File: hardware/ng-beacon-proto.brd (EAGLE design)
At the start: 71.1 x 76.2 mm, 6 parts

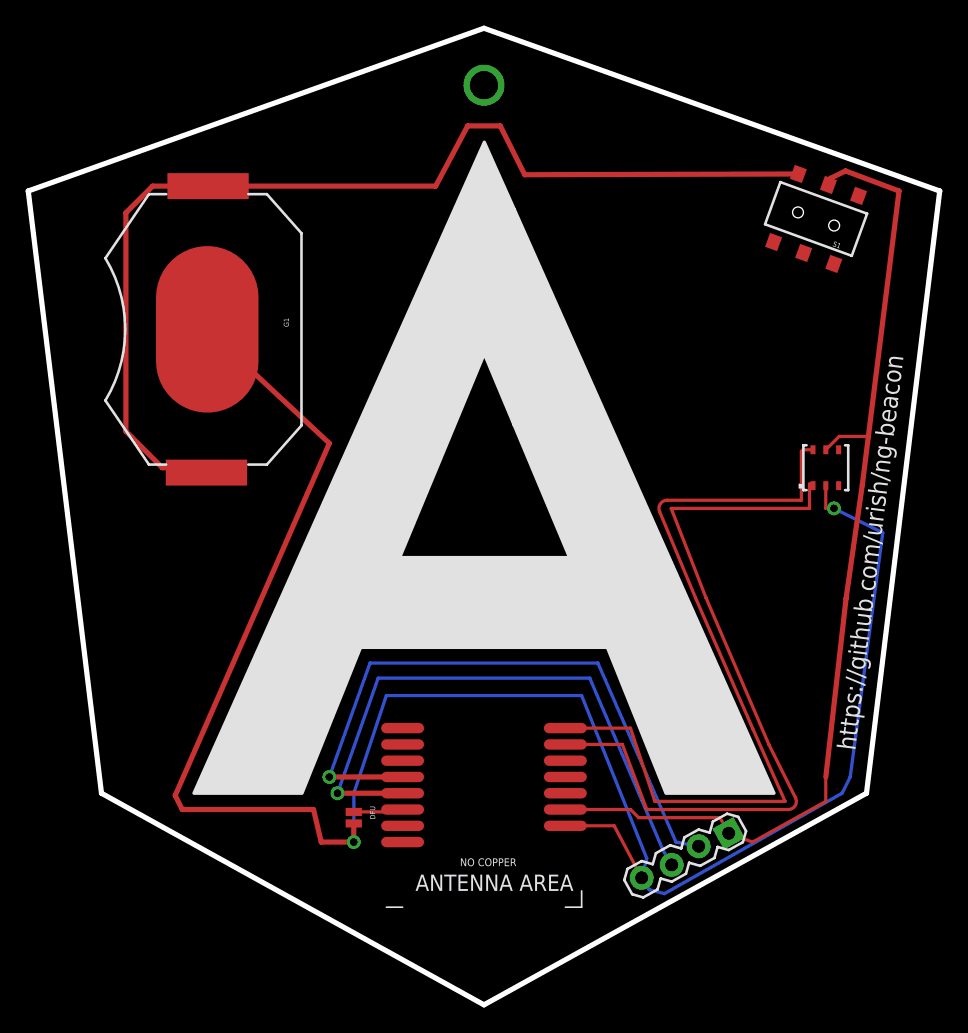
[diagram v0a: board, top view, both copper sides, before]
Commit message: move the proto version of a different file
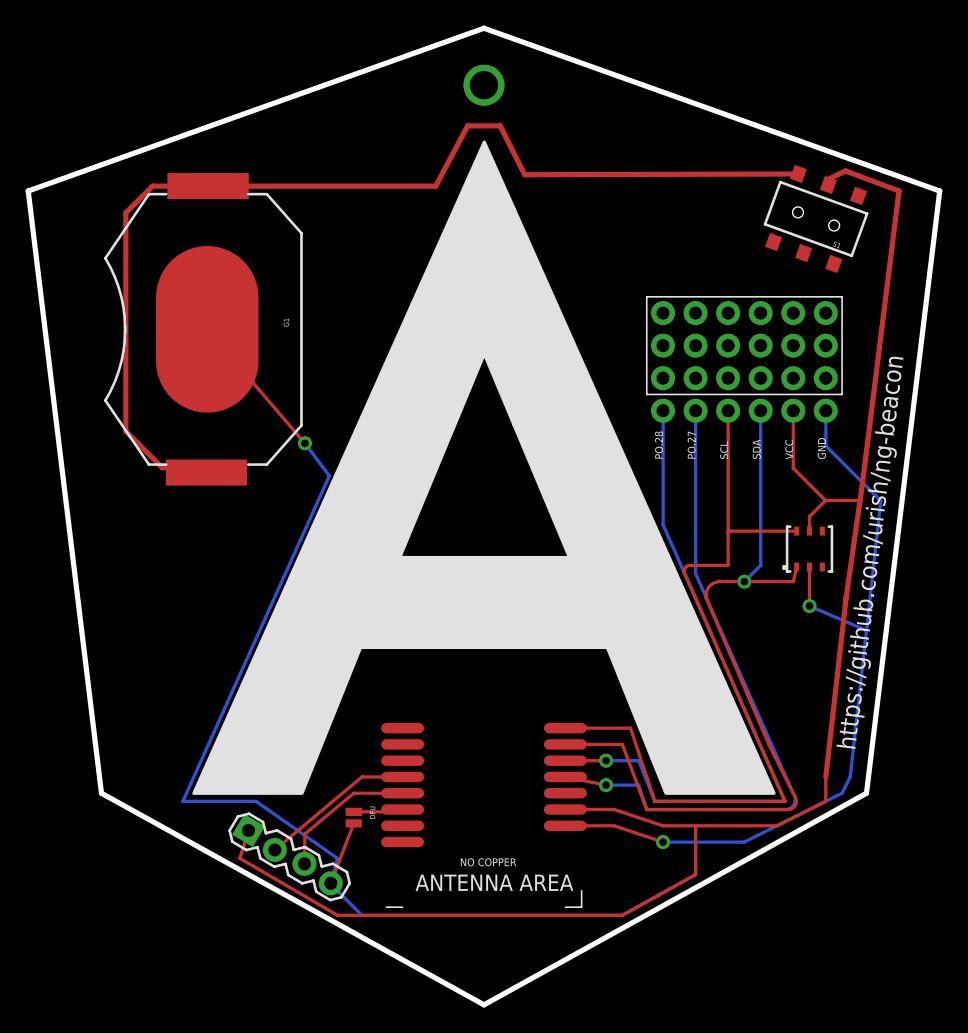
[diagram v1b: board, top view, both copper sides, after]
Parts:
- added J3: (no value), ng-beacon:PROTO4X6
- G1: device SparkFun-Electromechanical:BATTCON_20MM_4LEGS -> ng-beacon:BATTCON_20MM_4LEGS
- S1: device SparkFun-Electromechanical:AYZ0202 -> ng-beacon:AYZ0202
- SN1: device sensirion:DFN6/SHT -> ng-beacon:DFN6/SHT
- U$1: value PTR5518STD -> PTR5618; device PTR5518:PTR5518 -> ng-beacon:PTR5518
- moved J1 37.5 mm to (27.3, 12.2), turned to 329.2 degrees
- moved SN1 6.48 mm to (71.1, 34.3)
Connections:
- new net N$5: J3.P$2, U$1.12
- new net N$6: J3.P$1, U$1.13
- net GND: now also J3.P$6; no longer U$1.8
- net SCL: now also J3.P$3
- net SDA: now also J3.P$4
- net VIN: now also J3.P$5
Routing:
- net VIN: track 80.3 -> 132.6 mm
- net N$6: track 0.00 -> 51.8 mm, vias 0 -> 1
- net N$5: track 0.00 -> 51.5 mm, vias 0 -> 1
- net SWDIO: track 50.0 -> 12.0 mm, vias 1 -> 0
- net SWCLK: track 47.0 -> 11.1 mm, vias 1 -> 0
- net SDA: track 59.6 -> 61.5 mm, vias 0 -> 1
- net GND: track 157.4 -> 158.6 mm, vias 2 -> 3
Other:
- board text added: "GND"
- board text added: "PO.27"
- board text added: "PO.28"
- board text added: "SCL"
- board text added: "SDA"
- board text added: "VCC"

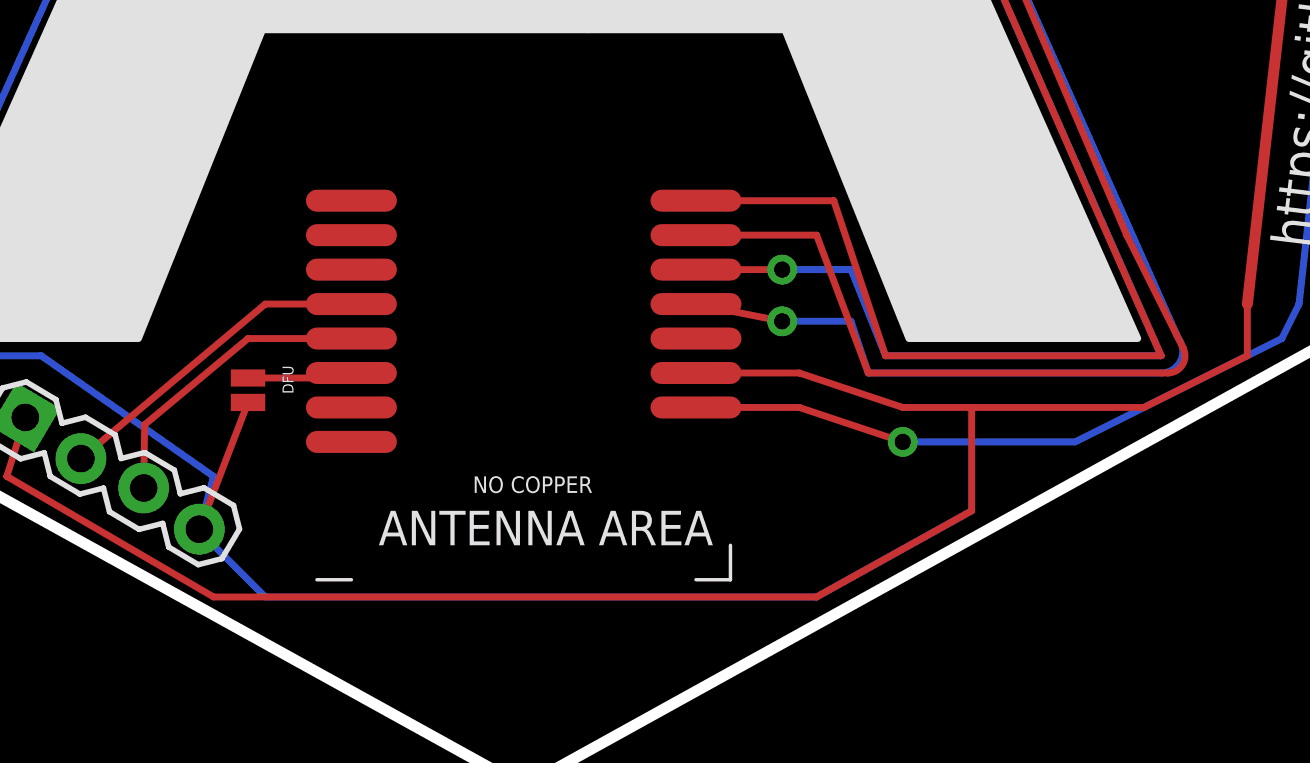
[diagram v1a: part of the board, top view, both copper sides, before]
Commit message: feat: add LED + BUTTON to the proto board
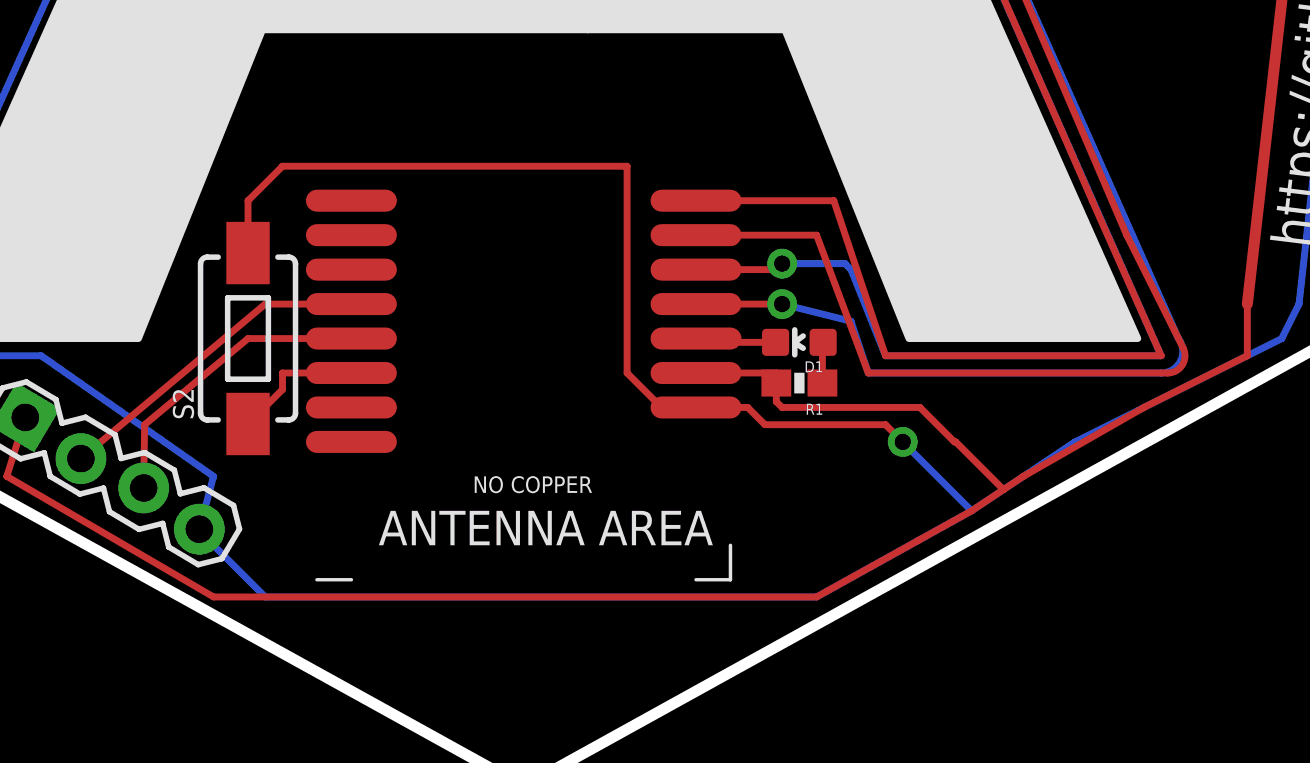
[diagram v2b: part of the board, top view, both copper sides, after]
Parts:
- removed DFU: JUMPER-PAD-2-NO, SparkFun-Passives:PAD-JUMPER-2-NO_NO_SILK
- added D1: GREEN, SparkFun-LED:LED-0603
- added R1: 470, SparkFun-Resistors:0603-RES
- added S2: SWITCH-MOMENTARY-2SMD-1101NE, SparkFun-Electromechanical:TACTILE-SWITCH-1101NE
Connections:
- new net N$7: D1.C, U$1.11
- new net N$8: D1.A, R1.1
- net GND: now also S2.2; no longer DFU.2
- net N$4: now also S2.1; no longer DFU.1
- net VIN: now also R1.2
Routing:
- net GND: track 158.6 -> 180.3 mm
- net N$7: track 0.00 -> 2.99 mm
- net N$8: track 0.00 -> 1.51 mm
- net N$4: track 3.99 -> 4.95 mm
- net VIN: track 132.6 -> 133.2 mm
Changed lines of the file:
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@@
 <?xml version="1.0" encoding="utf-8"?>
 <!DOCTYPE eagle SYSTEM "eagle.dtd">
-<eagle version="8.0.2">
+<eagle version="7.6.0">
 <drawing>
 <settings>
@@
 <attribute name="VALUE" x="73.995" y="32.415" size="0.8128" layer="27" ratio="10" rot="R90"/>
 </element>
-<element name="DFU" library="SparkFun-Passives" package="PAD-JUMPER-2-NO_NO_SILK" value="JUMPER-PAD-2-NO" x="35.56" y="13.335" rot="R270"/>
 <element name="J3" library="ng-beacon" package="PROTO4X6" value="" x="59.69" y="45.085" rot="R90"/>
+<element name="D1" library="SparkFun-LED" package="LED-0603" value="GREEN" x="55.88" y="15.1" rot="R90">
+<attribute name="PROD_ID" value="DIO-00821" x="55.88" y="15.1" size="1.778" layer="27" rot="R90" display="off"/>
+</element>
+<element name="R1" library="SparkFun-Resistors" package="0603-RES" value="470" x="55.88" y="13.6" rot="R180">
+<attribute name="PROD_ID" value="RES-07869" x="55.88" y="13.6" size="1.778" layer="27" rot="R180" display="off"/>
+</element>
+<element name="S2" library="SparkFun-Electromechanical" package="TACTILE-SWITCH-1101NE" value="SWITCH-MOMENTARY-2SMD-1101NE" x="35.56" y="15.24" rot="R90">
+<attribute name="PROD_ID" value="SWCH-00815" x="35.56" y="15.24" size="1.778" layer="27" rot="R90" display="off"/>
+</element>
 </elements>
 <signals>
@@
 <wire x1="75.565" y1="27.94" x2="74.295" y2="16.51" width="0.254" layer="16"/>
 <wire x1="74.295" y1="16.51" x2="73.66" y2="15.24" width="0.254" layer="16"/>
-<contactref element="DFU" pad="2"/>
 <wire x1="73.66" y1="15.24" x2="66.04" y2="11.43" width="0.254" layer="16"/>
-<wire x1="66.04" y1="11.43" x2="62.23" y2="11.43" width="0.254" layer="16"/>
+<wire x1="66.04" y1="11.43" x2="62.23" y2="8.89" width="0.254" layer="16"/>
 <via x="59.69" y="11.43" extent="1-16" drill="0.6" shape="square"/>
-<wire x1="62.23" y1="11.43" x2="59.69" y2="11.43" width="0.254" layer="16"/>
-<wire x1="59.69" y1="11.43" x2="55.88" y2="12.7" width="0.254" layer="1"/>
-<wire x1="55.88" y1="12.7" x2="52.07" y2="12.7" width="0.254" layer="1"/>
+<wire x1="62.23" y1="8.89" x2="59.69" y2="11.43" width="0.254" layer="16"/>
+<wire x1="53.975" y1="12.7" x2="52.07" y2="12.7" width="0.254" layer="1"/>
 <wire x1="33.76595" y1="8.213378125" x2="34.29" y2="10.16" width="0.254" layer="16"/>
 <wire x1="34.29" y1="10.16" x2="27.94" y2="14.605" width="0.254" layer="16"/>
@@
 <wire x1="76.68275" y1="38.046609375" x2="72.39" y2="42.339359375" width="0.254" layer="16"/>
 <wire x1="72.39" y1="42.339359375" x2="72.39" y2="45.085" width="0.254" layer="16"/>
-<wire x1="62.23" y1="11.43" x2="62.23" y2="8.89" width="0.254" layer="16"/>
 <wire x1="62.23" y1="8.89" x2="56.515" y2="5.715" width="0.254" layer="16"/>
 <wire x1="56.515" y1="5.715" x2="36.195" y2="5.715" width="0.254" layer="16"/>
-<wire x1="35.56" y1="12.885" x2="33.76595" y2="8.213378125" width="0.254" layer="1"/>
 <wire x1="36.195" y1="5.715" x2="33.76595" y2="8.14405" width="0.254" layer="16"/>
 <wire x1="33.76595" y1="8.14405" x2="33.76595" y2="8.213378125" width="0.254" layer="16"/>
+<wire x1="53.975" y1="12.7" x2="54.61" y2="12.065" width="0.254" layer="1"/>
+<wire x1="54.61" y1="12.065" x2="59.055" y2="12.065" width="0.254" layer="1"/>
+<wire x1="59.055" y1="12.065" x2="59.69" y2="11.43" width="0.254" layer="1"/>
+<contactref element="S2" pad="2"/>
+<wire x1="35.56" y1="18.39" x2="35.56" y2="20.32" width="0.254" layer="1"/>
+<wire x1="35.56" y1="20.32" x2="36.83" y2="21.59" width="0.254" layer="1"/>
+<wire x1="36.83" y1="21.59" x2="49.53" y2="21.59" width="0.254" layer="1"/>
+<wire x1="49.53" y1="21.59" x2="49.53" y2="13.97" width="0.254" layer="1"/>
+<wire x1="49.53" y1="13.97" x2="50.8" y2="12.7" width="0.254" layer="1"/>
+<wire x1="50.8" y1="12.7" x2="52.07" y2="12.7" width="0.254" layer="1"/>
 </signal>
 <signal name="N$1">
@@
 <wire x1="72.39" y1="16.51" x2="72.39" y2="14.605" width="0.254" layer="1"/>
 <wire x1="72.39" y1="14.605" x2="68.58" y2="12.7" width="0.254" layer="1"/>
-<wire x1="68.58" y1="12.7" x2="62.23" y2="12.7" width="0.254" layer="1"/>
-<wire x1="62.23" y1="12.7" x2="59.69" y2="12.7" width="0.254" layer="1"/>
-<wire x1="59.69" y1="12.7" x2="55.88" y2="13.97" width="0.254" layer="1"/>
-<wire x1="55.88" y1="13.97" x2="52.07" y2="13.97" width="0.254" layer="1"/>
-<wire x1="62.23" y1="12.7" x2="62.23" y2="8.89" width="0.254" layer="1"/>
-<wire x1="62.23" y1="8.89" x2="56.515" y2="5.715" width="0.254" layer="1"/>
+<wire x1="68.58" y1="12.7" x2="64.135" y2="10.16" width="0.254" layer="1"/>
+<wire x1="64.135" y1="10.16" x2="63.40230625" y2="9.6715375" width="0.254" layer="1"/>
+<wire x1="63.40230625" y1="9.6715375" x2="62.23" y2="8.89" width="0.254" layer="1"/>
+<wire x1="62.23" y1="8.89" x2="60.28905625" y2="7.811696875" width="0.254" layer="1"/>
+<wire x1="60.28905625" y1="7.811696875" x2="56.515" y2="5.715" width="0.254" layer="1"/>
 <wire x1="34.29" y1="5.715" x2="26.67" y2="10.16" width="0.254" layer="1"/>
 <wire x1="56.515" y1="5.715" x2="34.29" y2="5.715" width="0.254" layer="1"/>
@@
 <wire x1="69.85" y1="40.60170625" x2="69.85" y2="45.085" width="0.254" layer="1"/>
 <wire x1="72.370853125" y1="38.080853125" x2="69.85" y2="40.60170625" width="0.254" layer="1"/>
+<contactref element="R1" pad="2"/>
+<wire x1="52.07" y1="13.97" x2="55.03" y2="13.97" width="0.254" layer="1"/>
+<wire x1="55.03" y1="13.97" x2="55.03" y2="13.6" width="0.254" layer="1"/>
+<wire x1="55.03" y1="13.6" x2="55.03" y2="12.915" width="0.254" layer="1"/>
+<wire x1="55.03" y1="12.915" x2="55.245" y2="12.7" width="0.254" layer="1"/>
+<wire x1="55.245" y1="12.7" x2="60.325" y2="12.7" width="0.254" layer="1"/>
+<wire x1="60.325" y1="12.7" x2="61.595" y2="11.43" width="0.254" layer="1"/>
+<wire x1="61.595" y1="11.43" x2="61.64384375" y2="11.43" width="0.254" layer="1"/>
+<wire x1="61.64384375" y1="11.43" x2="63.40230625" y2="9.6715375" width="0.254" layer="1"/>
 </signal>
 <signal name="SWCLK">
@@
 <signal name="N$2">
 </signal>
-<signal name="N$4">
-<contactref element="U$1" pad="6"/>
-<contactref element="DFU" pad="1"/>
-<wire x1="35.56" y1="13.785" x2="39.37" y2="13.785" width="0.254" layer="1"/>
-<wire x1="39.37" y1="13.785" x2="39.37" y2="13.97" width="0.254" layer="1"/>
-</signal>
 <signal name="N$5">
 <contactref element="U$1" pad="12"/>
-<wire x1="52.07" y1="16.51" x2="55.245" y2="15.875" width="0.254" layer="1"/>
-<via x="55.245" y="15.875" extent="1-16" drill="0.6" shape="square"/>
-<wire x1="55.245" y1="15.875" x2="57.785" y2="15.875" width="0.254" layer="16"/>
+<wire x1="52.07" y1="16.51" x2="55.245" y2="16.51" width="0.254" layer="1"/>
+<via x="55.245" y="16.51" extent="1-16" drill="0.6" shape="square"/>
+<wire x1="55.245" y1="16.51" x2="57.785" y2="15.875" width="0.254" layer="16"/>
 <wire x1="57.785" y1="15.875" x2="58.42" y2="13.97" width="0.254" layer="16"/>
 <wire x1="58.42" y1="13.97" x2="69.215" y2="13.97" width="0.254" layer="16"/>
@@
 <signal name="N$6">
 <contactref element="U$1" pad="13"/>
-<wire x1="52.07" y1="17.78" x2="55.245" y2="17.78" width="0.254" layer="1"/>
-<via x="55.245" y="17.78" extent="1-16" drill="0.6" shape="square"/>
-<wire x1="55.245" y1="17.78" x2="57.785" y2="17.78" width="0.254" layer="16"/>
+<via x="55.245" y="18" extent="1-16" drill="0.6" shape="square"/>
 <wire x1="57.785" y1="17.78" x2="59.055" y2="14.605" width="0.254" layer="16"/>
 <wire x1="59.055" y1="14.605" x2="69.215" y2="14.605" width="0.254" layer="16"/>
@@
 <contactref element="J3" pad="P$1"/>
 <wire x1="59.69" y1="36.195" x2="59.69" y2="45.085" width="0.254" layer="16"/>
+<wire x1="52.07" y1="17.78" x2="55.025" y2="17.78" width="0.254" layer="1"/>
+<wire x1="55.025" y1="17.78" x2="55.245" y2="18" width="0.254" layer="1"/>
+<wire x1="55.245" y1="18" x2="57.565" y2="18" width="0.254" layer="16"/>
+<wire x1="57.565" y1="18" x2="57.785" y2="17.78" width="0.254" layer="16"/>
+</signal>
+<signal name="N$7">
+<contactref element="U$1" pad="11"/>
+<contactref element="D1" pad="C"/>
+<wire x1="55.003" y1="15.1" x2="52.21" y2="15.1" width="0.254" layer="1"/>
+<wire x1="52.21" y1="15.1" x2="52.07" y2="15.24" width="0.254" layer="1"/>
+</signal>
+<signal name="N$8">
+<contactref element="D1" pad="A"/>
+<contactref element="R1" pad="1"/>
+<wire x1="56.73" y1="13.6" x2="56.73" y2="15.073" width="0.254" layer="1"/>
+<wire x1="56.73" y1="15.073" x2="56.757" y2="15.1" width="0.254" layer="1"/>
+</signal>
+<signal name="N$4">
+<contactref element="U$1" pad="6"/>
+<contactref element="S2" pad="1"/>
+<wire x1="39.37" y1="13.97" x2="36.83" y2="13.97" width="0.254" layer="1"/>
+<wire x1="36.83" y1="13.97" x2="36.83" y2="13.36" width="0.254" layer="1"/>
+<wire x1="36.83" y1="13.36" x2="35.56" y2="12.09" width="0.254" layer="1"/>
 </signal>
 </signals>
